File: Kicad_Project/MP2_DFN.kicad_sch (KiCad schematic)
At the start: 240 parts, among them J1 Conn_01x07, J2 Conn_01x06, J3 Conn_01x06, J4 Conn_01x06, U1 TF2190-TAH, U2 TF2190-TAH, U3 TF2190-TAH, U4 NCS20034DR2G, U5 STM32F401CCU6_Balckpill, U6 PQDE6W-Q110 / RD5-110S12W, U7 12_DCDC_5

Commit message: added caps, prettied up phase connectors
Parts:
- removed CD7, CD8, CD9: 4.7uF, Capacitor_SMD:C_1210_3225Metric, symbol Device:C
- removed TpVBAT6: TestPoint, Busbars:my_testpoint_D1.7mm, symbol Connector:TestPoint
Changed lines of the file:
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@@
   (junction (at 486.41 156.21) (diameter 0) (color 0 0 0 0)
   )
-  (junction (at 179.705 43.815) (diameter 0) (color 0 0 0 0)
-  )
   (junction (at 452.755 76.2) (diameter 0) (color 0 0 0 0)
   )
@@
   (junction (at 130.048 155.702) (diameter 0) (color 0 0 0 0)
   )
-  (junction (at 401.32 368.3) (diameter 0) (color 0 0 0 0)
-  )
   (junction (at 41.91 78.74) (diameter 0) (color 0 0 0 0)
   )
@@
   (junction (at 491.49 328.93) (diameter 0) (color 0 0 0 0)
   )
-  (junction (at 159.385 43.815) (diameter 0) (color 0 0 0 0)
-  )
   (junction (at 534.67 241.3) (diameter 0) (color 0 0 0 0)
   )
@@
   (junction (at 443.23 59.69) (diameter 0) (color 0 0 0 0)
   )
-  (junction (at 179.705 28.575) (diameter 0) (color 0 0 0 0)
-  )
   (junction (at 538.48 80.01) (diameter 0) (color 0 0 0 0)
   )
@@
   (junction (at 246.38 46.99) (diameter 0) (color 0 0 0 0)
   )
-  (junction (at 169.545 43.815) (diameter 0) (color 0 0 0 0)
-  )
   (junction (at 451.485 241.3) (diameter 0) (color 0 0 0 0)
   )
@@
   (junction (at 466.725 229.87) (diameter 0) (color 0 0 0 0)
   )
-  (junction (at 169.545 28.575) (diameter 0) (color 0 0 0 0)
-  )
   (junction (at 474.98 180.975) (diameter 0) (color 0 0 0 0)
   )
@@
   (junction (at 140.97 133.35) (diameter 0) (color 0 0 0 0)
   )
-  (junction (at 159.385 28.575) (diameter 0) (color 0 0 0 0)
-  )
   (junction (at 406.4 360.68) (diameter 0) (color 0 0 0 0)
   )
@@
     (stroke (width 0) (type default))
   )
-  (wire (pts (xy 159.385 43.815) (xy 169.545 43.815))
-    (stroke (width 0) (type default))
-  )
   (wire (pts (xy 159.385 28.575) (xy 159.385 31.115))
     (stroke (width 0) (type default))
@@
     (stroke (width 0) (type default))
   )
-  (wire (pts (xy 401.32 368.3) (xy 388.62 368.3))
-    (stroke (width 0) (type default))
-  )
   (wire (pts (xy 260.35 151.13) (xy 275.59 151.13))
     (stroke (width 0) (type default))
@@
     (stroke (width 0) (type default))
   )
-  (wire (pts (xy 179.705 43.815) (xy 189.865 43.815))
-    (stroke (width 0) (type default))
-  )
   (wire (pts (xy 86.36 63.5) (xy 86.36 67.31))
     (stroke (width 0) (type default))
@@
     (stroke (width 0) (type default))
   )
-  (wire (pts (xy 179.705 38.735) (xy 179.705 43.815))
-    (stroke (width 0) (type default))
-  )
   (wire (pts (xy 243.84 33.02) (xy 246.38 33.02))
     (stroke (width 0) (type default))
@@
     (stroke (width 0) (type default))
   )
-  (wire (pts (xy 179.705 28.575) (xy 189.865 28.575))
-    (stroke (width 0) (type default))
-  )
   (wire (pts (xy 104.14 241.3) (xy 110.49 241.3))
     (stroke (width 0) (type default))
@@
     (stroke (width 0) (type default))
   )
-  (wire (pts (xy 169.545 43.815) (xy 179.705 43.815))
-    (stroke (width 0) (type default))
-  )
   (wire (pts (xy 466.09 148.59) (xy 466.725 148.59))
     (stroke (width 0) (type default))
@@
     (stroke (width 0) (type default))
   )
-  (wire (pts (xy 189.865 38.735) (xy 189.865 43.815))
-    (stroke (width 0) (type default))
-  )
   (wire (pts (xy 448.31 160.02) (xy 448.31 176.53))
     (stroke (width 0) (type default))
@@
     (stroke (width 0) (type default))
   )
-  (wire (pts (xy 406.4 368.3) (xy 401.32 368.3))
+  (wire (pts (xy 388.62 368.3) (xy 406.4 368.3))
     (stroke (width 0) (type default))
   )
@@
     (stroke (width 0) (type default))
   )
-  (wire (pts (xy 169.545 28.575) (xy 169.545 31.115))
-    (stroke (width 0) (type default))
-  )
   (wire (pts (xy 60.96 119.38) (xy 60.96 121.92))
     (stroke (width 0) (type default))
@@
     (stroke (width 0) (type default))
   )
-  (wire (pts (xy 179.705 28.575) (xy 179.705 31.115))
-    (stroke (width 0) (type default))
-  )
   (wire (pts (xy 504.19 140.97) (xy 504.19 143.51))
     (stroke (width 0) (type default))
@@
     (stroke (width 0) (type default))
   )
-  (wire (pts (xy 159.385 28.575) (xy 169.545 28.575))
-    (stroke (width 0) (type default))
-  )
   (wire (pts (xy 518.795 152.4) (xy 518.16 152.4))
     (stroke (width 0) (type default))
@@
     (stroke (width 0) (type default))
   )
-  (wire (pts (xy 169.545 28.575) (xy 179.705 28.575))
-    (stroke (width 0) (type default))
-  )
   (wire (pts (xy 199.39 87.63) (xy 204.47 87.63))
     (stroke (width 0) (type default))
@@
     (stroke (width 0) (type default))
   )
-  (wire (pts (xy 189.865 28.575) (xy 189.865 31.115))
-    (stroke (width 0) (type default))
-  )
   (wire (pts (xy 440.69 314.96) (xy 440.69 318.77))
     (stroke (width 0) (type default))
@@
     (stroke (width 0) (type default))
   )
-  (wire (pts (xy 169.545 38.735) (xy 169.545 43.815))
-    (stroke (width 0) (type default))
-  )
   (wire (pts (xy 220.472 199.898) (xy 220.472 201.168))
     (stroke (width 0) (type default))
@@
     )
   )
-  (symbol (lib_id "Device:C") (at 189.865 34.925 0) (unit 1)
-    (in_bom yes) (on_board yes) (dnp no)
-    (property "Reference" "CD9" (at 191.135 32.385 0)
-      (effects (font (size 1.27 1.27)) (justify left))
-    )
-    (property "Value" "4.7uF" (at 191.135 37.465 0)
-      (effects (font (size 1.27 1.27)) (justify left))
-    )
-    (property "Footprint" "Capacitor_SMD:C_1210_3225Metric" (at 190.8302 38.735 0)
-      (effects (font (size 1.27 1.27)) hide)
-    )
-    (property "Datasheet" "~" (at 189.865 34.925 0)
-      (effects (font (size 1.27 1.27)) hide)
-    )
-    (property "MFR PT" "FS32X475K101EGG" (at 189.865 34.925 0)
-      (effects (font (size 1.27 1.27)) hide)
-    )
-    (property "LCSC" "C381466" (at 189.865 34.925 0)
-      (effects (font (size 1.27 1.27)) hide)
-    )
-    (pin "1")
-    (pin "2")
-    (instances
-      (project "MP2_DFN"
-        (path "/31a3399e-b0e0-4a61-aacb-f319bb9df4d3"
-          (reference "CD9") (unit 1)
-        )
-      )
-    )
-  )
   (symbol (lib_id "Device:R") (at 534.67 185.42 180) (unit 1)
     (in_bom yes) (on_board yes) (dnp no)
@@
     )
   )
-  (symbol (lib_id "Connector:TestPoint") (at 401.32 368.3 0) (mirror y) (unit 1)
-    (in_bom no) (on_board yes) (dnp no)
-    (property "Reference" "TpVBAT6" (at 398.78 363.7279 0)
-      (effects (font (size 1.27 1.27)) (justify left))
-    )
-    (property "Value" "TestPoint" (at 398.78 366.2679 0)
-      (effects (font (size 1.27 1.27)) (justify left))
-    )
-    (property "Footprint" "Busbars:my_testpoint_D1.7mm" (at 396.24 368.3 0)
-      (effects (font (size 1.27 1.27)) hide)
-    )
-    (property "Datasheet" "~" (at 396.24 368.3 0)
-      (effects (font (size 1.27 1.27)) hide)
-    )
-    (pin "1")
-    (instances
-      (project "MP2_DFN"
-        (path "/31a3399e-b0e0-4a61-aacb-f319bb9df4d3"
-          (reference "TpVBAT6") (unit 1)
-        )
-      )
-    )
-  )
   (symbol (lib_id "Device:C") (at 77.47 71.12 0) (unit 1)
     (in_bom yes) (on_board yes) (dnp no)
@@
     )
   )
-  (symbol (lib_id "Device:C") (at 179.705 34.925 0) (unit 1)
-    (in_bom yes) (on_board yes) (dnp no)
-    (property "Reference" "CD8" (at 180.975 32.385 0)
-      (effects (font (size 1.27 1.27)) (justify left))
-    )
-    (property "Value" "4.7uF" (at 180.975 37.465 0)
-      (effects (font (size 1.27 1.27)) (justify left))
-    )
-    (property "Footprint" "Capacitor_SMD:C_1210_3225Metric" (at 180.6702 38.735 0)
-      (effects (font (size 1.27 1.27)) hide)
-    )
-    (property "Datasheet" "~" (at 179.705 34.925 0)
-      (effects (font (size 1.27 1.27)) hide)
-    )
-    (property "MFR PT" "FS32X475K101EGG" (at 179.705 34.925 0)
-      (effects (font (size 1.27 1.27)) hide)
-    )
-    (property "LCSC" "C381466" (at 179.705 34.925 0)
-      (effects (font (size 1.27 1.27)) hide)
-    )
-    (pin "1")
-    (pin "2")
-    (instances
-      (project "MP2_DFN"
-        (path "/31a3399e-b0e0-4a61-aacb-f319bb9df4d3"
-          (reference "CD8") (unit 1)
-        )
-      )
-    )
-  )
   (symbol (lib_id "Device:R") (at 448.31 261.62 180) (unit 1)
     (in_bom no) (on_board yes) (dnp no)
@@
         )
       )
-    )
-  )
-  (symbol (lib_id "Device:C") (at 169.545 34.925 0) (unit 1)
-    (in_bom yes) (on_board yes) (dnp no)
-    (property "Reference" "CD7" (at 170.815 32.385 0)
-      (effects (font (size 1.27 1.27)) (justify left))
-    )
-    (property "Value" "4.7uF" (at 170.815 37.465 0)
-      (effects (font (size 1.27 1.27)) (justify left))
-    )
-    (property "Footprint" "Capacitor_SMD:C_1210_3225Metric" (at 170.5102 38.735 0)
-      (effects (font (size 1.27 1.27)) hide)
-    )
-    (property "Datasheet" "~" (at 169.545 34.925 0)
-      (effects (font (size 1.27 1.27)) hide)
-    )
-    (property "MFR PT" "FS32X475K101EGG" (at 169.545 34.925 0)
-      (effects (font (size 1.27 1.27)) hide)
-    )
-    (property "LCSC" "C381466" (at 169.545 34.925 0)
-      (effects (font (size 1.27 1.27)) hide)
-    )
-    (pin "1")
-    (pin "2")
-    (instances
-      (project "MP2_DFN"
-        (path "/31a3399e-b0e0-4a61-aacb-f319bb9df4d3"
-          (reference "CD7") (unit 1)
-        )
-      )

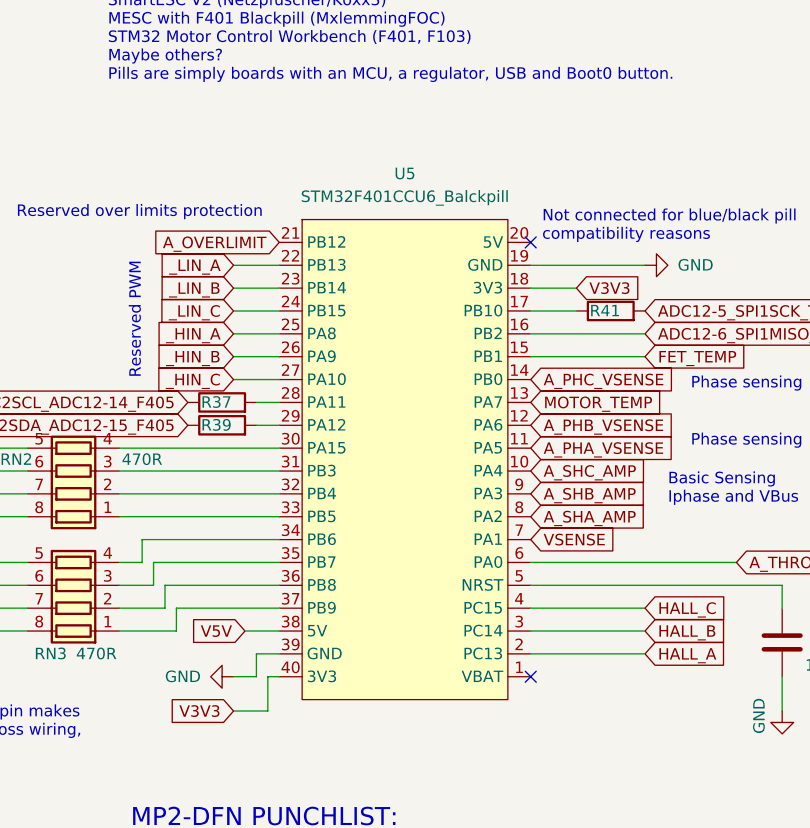
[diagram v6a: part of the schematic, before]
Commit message: changed schematic to F405 pill, cleanup on vias/tracks
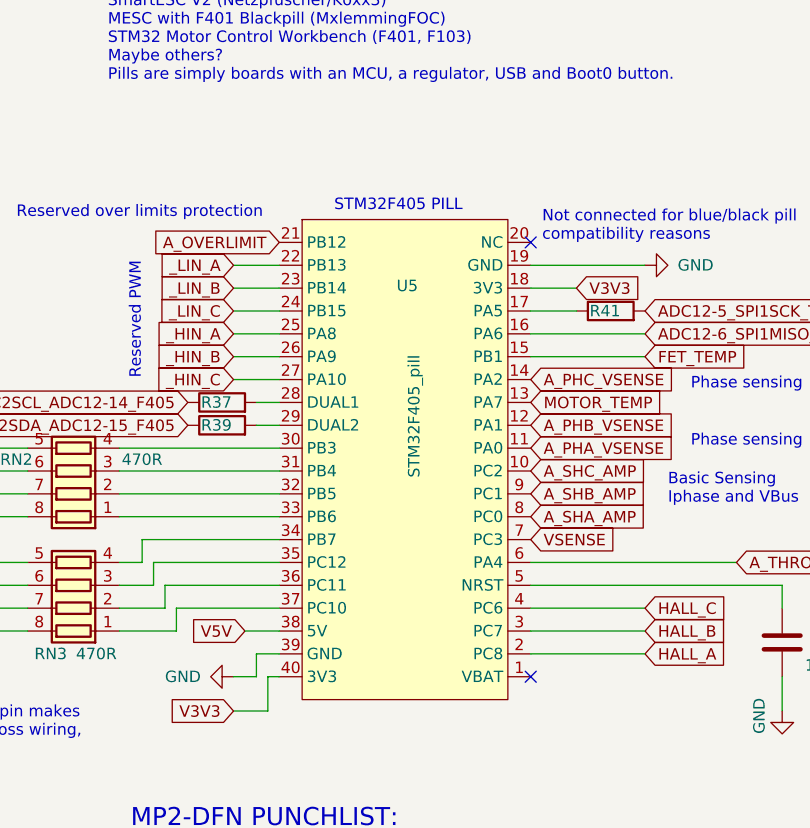
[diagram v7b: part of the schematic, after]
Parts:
- removed U5: STM32F401CCU6_Balckpill, MP2_DFN_Custom_parts:Blackpill_STM32F401CEU6, symbol MP2_DFN_Custom_Symbols:STM32F401CCU6_Balckpill
- added U5: STM32F405_pill, MP2_DFN_Custom_parts:STM32F405_pill, symbol CCC_ESC_Custom_Symbols:STM32F405_pill
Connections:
- net ADC12-6_SPI1MISO_TIM13CH1_F405: now also U5.16 (PA6)
- net A_OVERLIMIT: now also U5.21 (PB12)
- net A_PHA_VSENSE: now also U5.11 (PA0)
- net A_PHB_VSENSE: now also U5.12 (PA1)
- net A_PHC_VSENSE: now also U5.14 (PA2)
- net A_SHA_AMP: now also U5.8 (PC0)
- net A_SHB_AMP: now also U5.9 (PC1)
- net A_SHC_AMP: now also U5.10 (PC2)
- net A_THROTTLE: now also U5.6 (PA4)
- net FET_TEMP: now also U5.15 (PB1)
- net GND: now also U5.19 (GND), U5.39 (GND)
- net HALL_A: now also U5.2 (PC8)
- net HALL_B: now also U5.3 (PC7)
- net HALL_C: now also U5.4 (PC6)
- net MOTOR_TEMP: now also U5.13 (PA7)
- net V3V3: now also U5.18 (3V3), U5.40 (3V3)
- net V5V: now also U5.38 (5V)
- net VSENSE: now also U5.7 (PC3)
- net _HIN_A: now also U5.25 (PA8)
- net _HIN_B: now also U5.26 (PA9)
- net _HIN_C: now also U5.27 (PA10)
- net _LIN_A: now also U5.22 (PB13)
- net _LIN_B: now also U5.23 (PB14)
- net _LIN_C: now also U5.24 (PB15)
- net at R39.2: now also U5.29 (DUAL2)
- net at R41.1: now also U5.17 (PA5)
- net at R37.2: now also U5.28 (DUAL1)
- net at RN2.4 (R4.1): now also U5.30 (PB3)
- net at RN2.3 (R3.1): now also U5.31 (PB4)
- net at RN2.2 (R2.1): now also U5.32 (PB5)
- net at RN2.1 (R1.1): now also U5.33 (PB6)
- net at RN3.4 (R4.1): now also U5.34 (PB7)
- net at RN3.3 (R3.1): now also U5.35 (PC12)
- net at RN3.2 (R2.1): now also U5.36 (PC11)
- net at RN3.1 (R1.1): now also U5.37 (PC10)
- net at C21.1: now also U5.5 (NRST)
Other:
- note added: "STM32F405 PILL"
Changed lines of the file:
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@@
     (effects (font (size 1.27 1.27)) (justify left bottom))
   )
+  (text "STM32F405 PILL" (at 281.686 114.808 0)
+    (effects (font (size 1.27 1.27)) (justify left bottom))
+  )
   (text "Notes on power stage design:\n\nPulldowns optional, most gate drivers pull down the FETs when UVLO\nMOS should have good Ciss/Crss ratio\nCiss/Crss>Vbat minimises the chance of parasitic turn-on.\nTarget gate time constant ~200ns: \nRG = 1R8(fet) + 15R (ext) + 3R33/3 (gate driver)\nCiss = 11.4nF\nRC = 11.4nF x 16.9R = 192.66ns"
     (at 393.7 52.07 0)
@@
     )
   )
+  (symbol (lib_id "CCC_ESC_Custom_Symbols:STM32F405_pill") (at 278.13 115.57 0) (unit 1)
+    (in_bom no) (on_board yes) (dnp no)
+    (property "Reference" "U5" (at 289.814 122.936 0)
+      (effects (font (size 1.27 1.27)))
+    )
+    (property "Value" "STM32F405_pill" (at 290.576 137.414 90)
+      (effects (font (size 1.27 1.27)))
+    )
+    (property "Footprint" "MP2_DFN_Custom_parts:STM32F405_pill" (at 287.6804 113.4872 0)
+      (effects (font (size 1.27 1.27)) hide)
+    )
+    (property "Datasheet" "" (at 278.13 115.57 0)
+      (effects (font (size 1.27 1.27)) hide)
+    )
+    (property "DNP" "YES" (at 278.13 115.57 0)
+      (effects (font (size 1.27 1.27)) hide)
+    )
+    (pin "1")
+    (pin "10")
+    (pin "11")
+    (pin "12")
+    (pin "13")
+    (pin "14")
+    (pin "15")
+    (pin "16")
+    (pin "17")
+    (pin "18")
+    (pin "19")
+    (pin "2")
+    (pin "20")
+    (pin "21")
+    (pin "22")
+    (pin "23")
+    (pin "24")
+    (pin "25")
+    (pin "26")
+    (pin "27")
+    (pin "28")
+    (pin "29")
+    (pin "3")
+    (pin "30")
+    (pin "31")
+    (pin "32")
+    (pin "33")
+    (pin "34")
+    (pin "35")
+    (pin "36")
+    (pin "37")
+    (pin "38")
+    (pin "39")
+    (pin "4")
+    (pin "40")
+    (pin "5")
+    (pin "6")
+    (pin "7")
+    (pin "8")
+    (pin "9")
+    (instances
+      (project "MP2_DFN"
+        (path "/31a3399e-b0e0-4a61-aacb-f319bb9df4d3"
+          (reference "U5") (unit 1)
+        )
+      )
+      (project "F405_pill"
+        (path "/e63e39d7-6ac0-4ffd-8aa3-1841a4541b55"
+          (reference "U4") (unit 1)
+        )
+      )
+    )
+  )
   (symbol (lib_id "Device:R") (at 312.42 125.73 90) (unit 1)
     (in_bom yes) (on_board yes) (dnp no)
@@
         )
       )
-    )
-  )
-  (symbol (lib_id "MP2_DFN_Custom_Symbols:STM32F401CCU6_Balckpill") (at 278.13 115.57 0) (unit 1)
-    (in_bom no) (on_board yes) (dnp no) (fields_autoplaced)
-    (property "Reference" "U5" (at 289.56 110.49 0)
-      (effects (font (size 1.27 1.27)))
-    )
-    (property "Value" "STM32F401CCU6_Balckpill" (at 289.56 113.03 0)
-      (effects (font (size 1.27 1.27)))
-    )
-    (property "Footprint" "MP2_DFN_Custom_parts:Blackpill_STM32F401CEU6" (at 278.13 115.57 0)
-      (effects (font (size 1.27 1.27)) hide)
-    )
-    (property "Datasheet" "" (at 278.13 115.57 0)
-      (effects (font (size 1.27 1.27)) hide)
-    )
-    (pin "1")
-    (pin "10")
-    (pin "11")
-    (pin "12")
-    (pin "13")
-    (pin "14")
-    (pin "15")
-    (pin "16")
-    (pin "17")
-    (pin "18")
-    (pin "19")
-    (pin "2")
-    (pin "20")
-    (pin "21")
-    (pin "22")
-    (pin "23")
-    (pin "24")
-    (pin "25")
-    (pin "26")
-    (pin "27")
-    (pin "28")
-    (pin "29")
-    (pin "3")
-    (pin "30")
-    (pin "31")
-    (pin "32")
-    (pin "33")
-    (pin "34")
-    (pin "35")
-    (pin "36")
-    (pin "37")
-    (pin "38")
-    (pin "39")
-    (pin "4")
-    (pin "40")
-    (pin "5")
-    (pin "6")
-    (pin "7")
-    (pin "8")
-    (pin "9")
-    (instances
-      (project "MP2_DFN"
-        (path "/31a3399e-b0e0-4a61-aacb-f319bb9df4d3"
-          (reference "U5") (unit 1)
-        )
-      )
